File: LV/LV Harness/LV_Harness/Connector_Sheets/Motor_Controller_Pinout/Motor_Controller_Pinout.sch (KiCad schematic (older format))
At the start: 4 parts

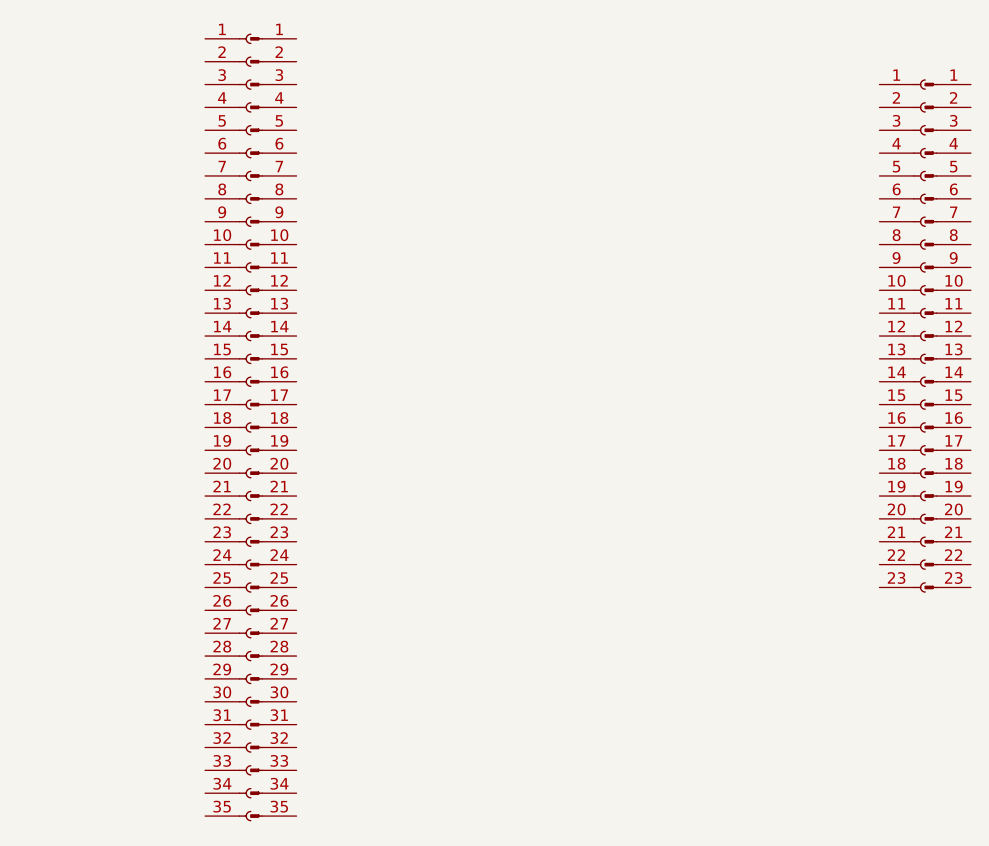
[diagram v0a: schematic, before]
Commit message: Motor Controller Pinouts labelled
The pins have been labelled
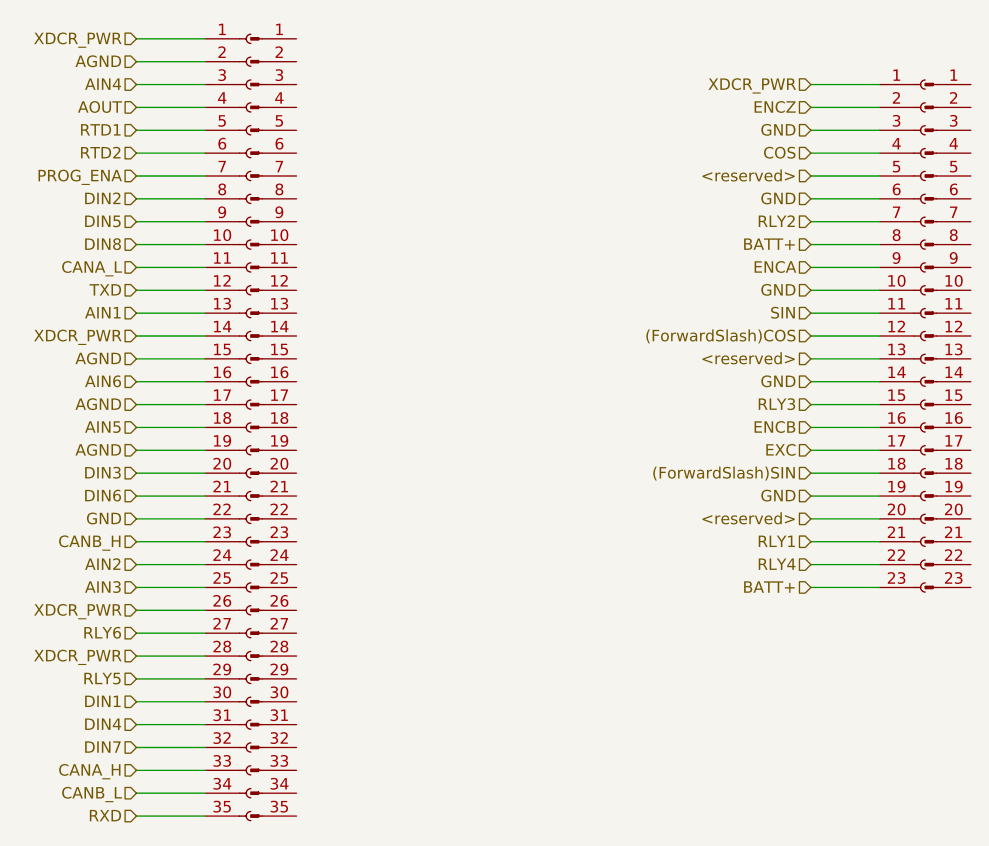
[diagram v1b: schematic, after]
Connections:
- net XDCR_PWR: now reaches J?.1 (Pin_1)
- net XDCR_PWR: now also J?.1 (Pin_1), J?.14 (Pin_14), J?.26 (Pin_26), J?.28 (Pin_28)
- net DIN8: now reaches J?.10 (Pin_10)
- net CANA_L: now reaches J?.11 (Pin_11)
- net TXD: now reaches J?.12 (Pin_12)
- net AIN1: now reaches J?.13 (Pin_13)
- net AGND: now reaches J?.15 (Pin_15)
- net AGND: now also J?.17 (Pin_17), J?.19 (Pin_19), J?.2 (Pin_2)
- net AIN6: now reaches J?.16 (Pin_16)
- net AIN5: now reaches J?.18 (Pin_18)
- net DIN3: now reaches J?.20 (Pin_20)
- net DIN6: now reaches J?.21 (Pin_21)
- net GND: now reaches J?.22 (Pin_22)
- net GND: now also J?.10 (Pin_10), J?.14 (Pin_14), J?.19 (Pin_19), J?.3 (Pin_3), J?.6 (Pin_6)
- net CANB_H: now reaches J?.23 (Pin_23)
- net AIN2: now reaches J?.24 (Pin_24)
- net AIN3: now reaches J?.25 (Pin_25)
- net RLY6: now reaches J?.27 (Pin_27)
- net RLY5: now reaches J?.29 (Pin_29)
- net AIN4: now reaches J?.3 (Pin_3)
- net DIN1: now reaches J?.30 (Pin_30)
- net DIN4: now reaches J?.31 (Pin_31)
- net DIN7: now reaches J?.32 (Pin_32)
- net CANA_H: now reaches J?.33 (Pin_33)
- net CANB_L: now reaches J?.34 (Pin_34)
- net RXD: now reaches J?.35 (Pin_35)
- net AOUT: now reaches J?.4 (Pin_4)
- net RTD1: now reaches J?.5 (Pin_5)
- net RTD2: now reaches J?.6 (Pin_6)
- net PROG_ENA: now reaches J?.7 (Pin_7)
- net DIN2: now reaches J?.8 (Pin_8)
- net DIN5: now reaches J?.9 (Pin_9)
- net SIN: now reaches J?.11 (Pin_11)
- net (ForwardSlash)COS: now reaches J?.12 (Pin_12)
- net <reserved>: now reaches J?.13 (Pin_13)
- net <reserved>: now also J?.20 (Pin_20), J?.5 (Pin_5)
- net RLY3: now reaches J?.15 (Pin_15)
- net ENCB: now reaches J?.16 (Pin_16)
- net EXC: now reaches J?.17 (Pin_17)
- net (ForwardSlash)SIN: now reaches J?.18 (Pin_18)
- net ENCZ: now reaches J?.2 (Pin_2)
- net RLY1: now reaches J?.21 (Pin_21)
- net RLY4: now reaches J?.22 (Pin_22)
- net BATT+: now reaches J?.23 (Pin_23)
- net BATT+: now also J?.8 (Pin_8)
- net COS: now reaches J?.4 (Pin_4)
- net RLY2: now reaches J?.7 (Pin_7)
- net ENCA: now reaches J?.9 (Pin_9)
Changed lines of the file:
@@
 EESchema Schematic File Version 4
-EELAYER 29 0
+EELAYER 30 0
 EELAYER END
 $Descr A4 11693 8268
@@
 	1    0    0    -1
 $EndComp
+Text HLabel 3800 2200 0    50   Input ~ 0
+XDCR_PWR
+Wire Wire Line
+	4100 2200 3800 2200
+Text HLabel 3800 2300 0    50   Input ~ 0
+AGND
+Wire Wire Line
+	4100 2300 3800 2300
+Text HLabel 3800 2400 0    50   Input ~ 0
+AIN4
+Wire Wire Line
+	4100 2400 3800 2400
+Text HLabel 3800 2500 0    50   Input ~ 0
+AOUT
+Wire Wire Line
+	4100 2500 3800 2500
+Text HLabel 3800 2600 0    50   Input ~ 0
+RTD1
+Wire Wire Line
+	4100 2600 3800 2600
+Text HLabel 3800 2700 0    50   Input ~ 0
+RTD2
+Wire Wire Line
+	4100 2700 3800 2700
+Text HLabel 3800 2800 0    50   Input ~ 0
+PROG_ENA
+Wire Wire Line
+	4100 2800 3800 2800
+Text HLabel 3800 2900 0    50   Input ~ 0
+DIN2
+Text HLabel 3800 3000 0    50   Input ~ 0
+DIN5
+Text HLabel 3800 3100 0    50   Input ~ 0
+DIN8
+Text HLabel 3800 3200 0    50   Input ~ 0
+CANA_L
+Text HLabel 3800 3300 0    50   Input ~ 0
+TXD
+Wire Wire Line
+	3800 2900 4100 2900
+Wire Wire Line
+	3800 3000 4100 3000
+Wire Wire Line
+	3800 3100 4100 3100
+Wire Wire Line
+	3800 3200 4100 3200
+Wire Wire Line
+	3800 3300 4100 3300
+Text HLabel 3800 3400 0    50   Input ~ 0
+AIN1
+Text HLabel 3800 3500 0    50   Input ~ 0
+XDCR_PWR
+Text HLabel 3800 3600 0    50   Input ~ 0
+AGND
+Text HLabel 3800 3700 0    50   Input ~ 0
+AIN6
+Text HLabel 3800 3800 0    50   Input ~ 0
+AGND
+Text HLabel 3800 3900 0    50   Input ~ 0
+AIN5
+Text HLabel 3800 4000 0    50   Input ~ 0
+AGND
+Text HLabel 3800 4100 0    50   Input ~ 0
+DIN3
+Text HLabel 3800 4200 0    50   Input ~ 0
+DIN6
+Text HLabel 3800 4300 0    50   Input ~ 0
+GND
+Text HLabel 3800 4400 0    50   Input ~ 0
+CANB_H
+Text HLabel 3800 4500 0    50   Input ~ 0
+AIN2
+Text HLabel 3800 4600 0    50   Input ~ 0
+AIN3
+Text HLabel 3800 4700 0    50   Input ~ 0
+XDCR_PWR
+Text HLabel 3800 4800 0    50   Input ~ 0
+RLY6
+Text HLabel 3800 4900 0    50   Input ~ 0
+XDCR_PWR
+Text HLabel 3800 5000 0    50   Input ~ 0
+RLY5
+Text HLabel 3800 5100 0    50   Input ~ 0
+DIN1
+Text HLabel 3800 5200 0    50   Input ~ 0
+DIN4
+Text HLabel 3800 5300 0    50   Input ~ 0
+DIN7
+Text HLabel 3800 5400 0    50   Input ~ 0
+CANA_H
+Text HLabel 3800 5500 0    50   Input ~ 0
+CANB_L
+Text HLabel 3800 5600 0    50   Input ~ 0
+RXD
+Wire Wire Line
+	3800 3400 4100 3400
+Wire Wire Line
+	3800 3500 4100 3500
+Wire Wire Line
+	3800 3600 4100 3600
+Wire Wire Line
+	3800 3700 4100 3700
+Wire Wire Line
+	3800 3800 4100 3800
+Wire Wire Line
+	3800 3900 4100 3900
+Wire Wire Line
+	3800 4000 4100 4000
+Wire Wire Line
+	3800 4100 4100 4100
+Wire Wire Line
+	3800 4200 4100 4200
+Wire Wire Line
+	3800 4300 4100 4300
+Wire Wire Line
+	3800 4400 4100 4400
+Wire Wire Line
+	3800 4500 4100 4500
+Wire Wire Line
+	3800 4600 4100 4600
+Wire Wire Line
+	3800 4700 4100 4700
+Wire Wire Line
+	3800 4800 4100 4800
+Wire Wire Line
+	3800 4900 4100 4900
+Wire Wire Line
+	3800 5000 4100 5000
+Wire Wire Line
+	3800 5100 4100 5100
+Wire Wire Line
+	3800 5200 4100 5200
+Wire Wire Line
+	3800 5300 4100 5300
+Wire Wire Line
+	3800 5400 4100 5400
+Wire Wire Line
+	3800 5500 4100 5500
+Wire Wire Line
+	3800 5600 4100 5600
+Text HLabel 6750 2400 0    50   Input ~ 0
+XDCR_PWR
+Text HLabel 6750 2500 0    50   Input ~ 0
+ENCZ
+Text HLabel 6750 2600 0    50   Input ~ 0
+GND
+Text HLabel 6750 2700 0    50   Input ~ 0
+COS
+Text HLabel 6750 2800 0    50   Input ~ 0
+<reserved>
+Text HLabel 6750 2900 0    50   Input ~ 0
+GND
+Text HLabel 6750 3000 0    50   Input ~ 0
+RLY2
+Text HLabel 6750 3100 0    50   Input ~ 0
+BATT+
+Text HLabel 6750 3200 0    50   Input ~ 0
+ENCA
+Text HLabel 6750 3300 0    50   Input ~ 0
+GND
+Text HLabel 6750 3400 0    50   Input ~ 0
+SIN
+Text HLabel 6750 3500 0    50   Input ~ 0
+(ForwardSlash)COS
+Text HLabel 6750 3600 0    50   Input ~ 0
+<reserved>
+Text HLabel 6750 3700 0    50   Input ~ 0
+GND
+Text HLabel 6750 3800 0    50   Input ~ 0
+RLY3
+Text HLabel 6750 3900 0    50   Input ~ 0
+ENCB
+Text HLabel 6750 4000 0    50   Input ~ 0
+EXC
+Text HLabel 6750 4100 0    50   Input ~ 0
+(ForwardSlash)SIN
+Text HLabel 6750 4200 0    50   Input ~ 0
+GND
+Text HLabel 6750 4300 0    50   Input ~ 0
+<reserved>
+Text HLabel 6750 4400 0    50   Input ~ 0
+RLY1
+Text HLabel 6750 4500 0    50   Input ~ 0
+RLY4
+Text HLabel 6750 4600 0    50   Input ~ 0
+BATT+
+Wire Wire Line
+	6750 2400 7050 2400
+Wire Wire Line
+	6750 2500 7050 2500
+Wire Wire Line
+	6750 2600 7050 2600
+Wire Wire Line
+	6750 2700 7050 2700
+Wire Wire Line
+	6750 2800 7050 2800
+Wire Wire Line
+	6750 2900 7050 2900
+Wire Wire Line
+	6750 3000 7050 3000
+Wire Wire Line
+	6750 3100 7050 3100
+Wire Wire Line
+	6750 3200 7050 3200
+Wire Wire Line
+	6750 3300 7050 3300
+Wire Wire Line
+	6750 3400 7050 3400
+Wire Wire Line
+	6750 3500 7050 3500
+Wire Wire Line
+	6750 3600 7050 3600
+Wire Wire Line
+	6750 3700 7050 3700
+Wire Wire Line
+	6750 3800 7050 3800
+Wire Wire Line
+	6750 3900 7050 3900
+Wire Wire Line
+	6750 4000 7050 4000
+Wire Wire Line
+	6750 4100 7050 4100
+Wire Wire Line
+	6750 4200 7050 4200
+Wire Wire Line
+	6750 4300 7050 4300
+Wire Wire Line
+	6750 4400 7050 4400
+Wire Wire Line
+	6750 4500 7050 4500
+Wire Wire Line
+	6750 4600 7050 4600
 $EndSCHEMATC
